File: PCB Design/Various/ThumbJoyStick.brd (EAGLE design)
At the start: 21.6 x 14 mm, 5 parts

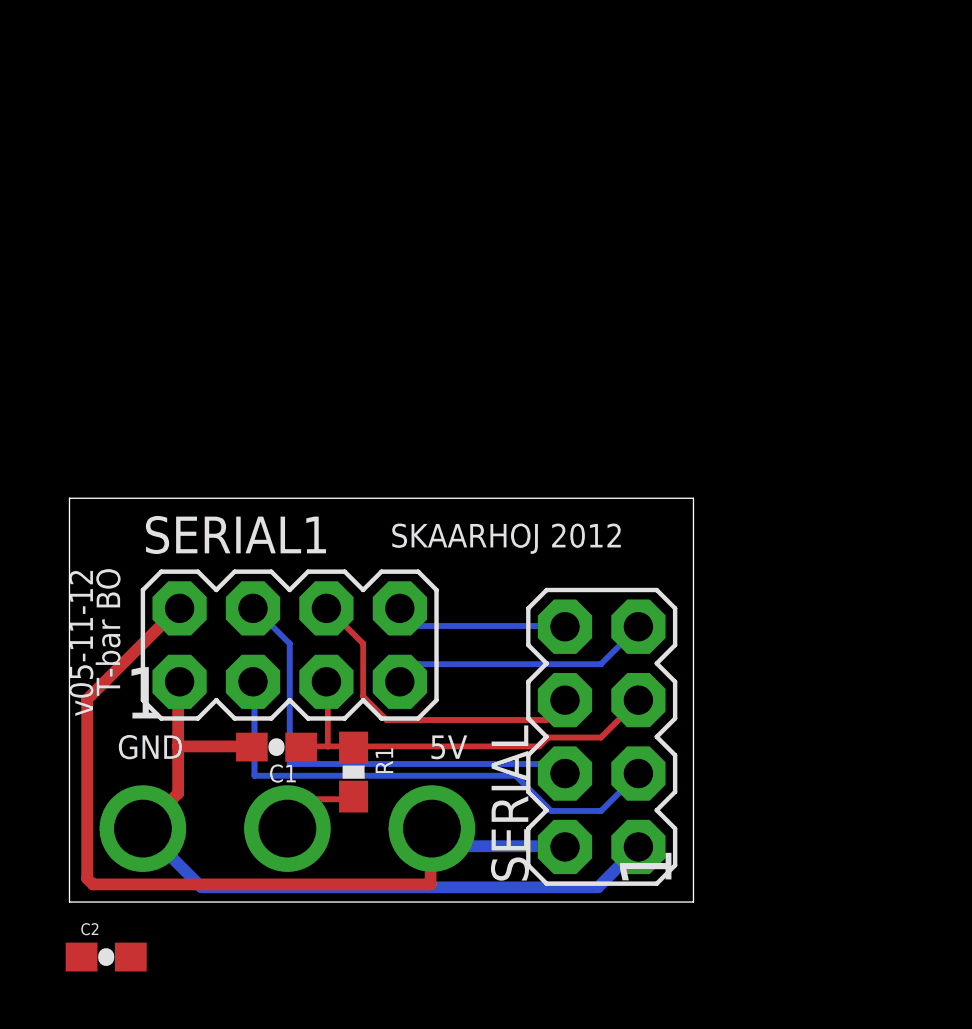
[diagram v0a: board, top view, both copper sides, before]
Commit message: Numerous updates to PCBs including a whole new design, C330 (in the making)
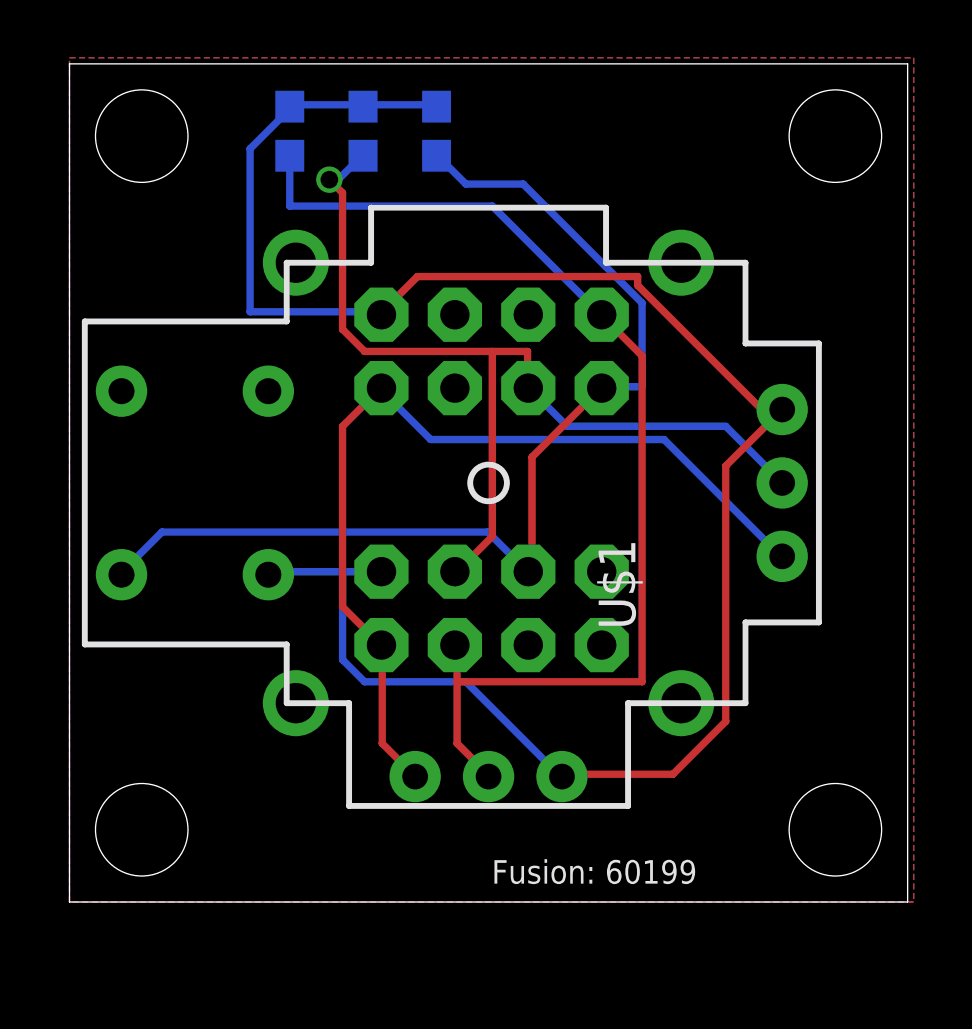
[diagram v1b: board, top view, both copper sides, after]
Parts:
- removed R1: 10K, SparkFun:0603-RES
- removed SERIAL, SERIAL1: M04X2, SparkFun:2X4
- added C3: 10nF, SparkFun:0603-CAP
- added JOY1, JOY2: M04X2, SparkFun:2X4
- added U$1: PLAYSTATION2_ANALOG_JOYSTICK, SKAARHOJ:PLAYSTATION2_ANALOG_JOYSTICK
- C1: value 1uF -> 10nF
- C2: value 10uF -> 10nF
- moved C2 29.9 mm to (10.2, 26.7), flipped to the bottom, turned to 90 degrees
- moved C1 21.3 mm to (7.62, 26.7), flipped to the bottom, turned to 90 degrees
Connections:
- removed net DISP_DATA_OUT: SERIAL.6, SERIAL1.6
- removed net I2C_SCL: SERIAL.4, SERIAL1.4
- removed net I2C_SDA: SERIAL.3, SERIAL1.3
- removed net SDI_MOSI: SERIAL.8, SERIAL1.8
- removed net SDI_SCLK: SERIAL.7, SERIAL1.7
- removed net SLIDER_IN: C1.1, R1.1, SERIAL.5, SERIAL1.5
- removed net T-BAR: R1.2
- new net POT1: C1.1, JOY1.2, JOY2.5, U$1.V2
- new net POT2: C2.1, JOY1.3, JOY2.6, U$1.H2
- new net SW: C3.1, JOY1.1, JOY2.4, U$1.B1A
- net 5V: now also JOY1.7, JOY2.7, U$1.H1, U$1.V1; no longer C2.1, SERIAL.2, SERIAL1.2
- net GND: now also C3.2, JOY1.8, JOY2.8, U$1.B2A, U$1.H3, U$1.V3; no longer SERIAL.1, SERIAL1.1
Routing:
- net GND: track 26.8 -> 68.5 mm, vias 1 -> 0
- net POT1: track 0.00 -> 38.8 mm
- net SW: track 0.00 -> 36.3 mm
- net POT2: track 0.00 -> 33.2 mm, vias 0 -> 1
- net I2C_SDA: track 17.6 -> 0.00 mm
- net I2C_SCL: track 15.6 -> 0.00 mm
- net SLIDER_IN: track 14.7 -> 0.00 mm
- net DISP_DATA_OUT: track 11.6 -> 0.00 mm
- net SDI_SCLK: track 9.04 -> 0.00 mm
- net SDI_MOSI: track 5.97 -> 0.00 mm
- net T-BAR: track 3.35 -> 0.00 mm, vias 1 -> 0
- net 5V: track 29.5 -> 31.4 mm, vias 1 -> 0
- added copper zone on layer 1, net GND
- added copper zone on layer 16, net GND
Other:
- board size 21.6 x 14 mm -> 29 x 29 mm
- board text added: "Fusion: 60199"
- board text removed: "1"
- board text removed: "5V"
- board text removed: "Fusion: 63103"
- board text removed: "GND"
- board text removed: "SKAARHOJ 2012"
- board text removed: "T-bar BO"
- board text removed: "v05-11-12"
